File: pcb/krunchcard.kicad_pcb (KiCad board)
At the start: 2 copper layers, 86 x 54 mm, 27 parts, among them U1 NT3H2111W0FTTJ

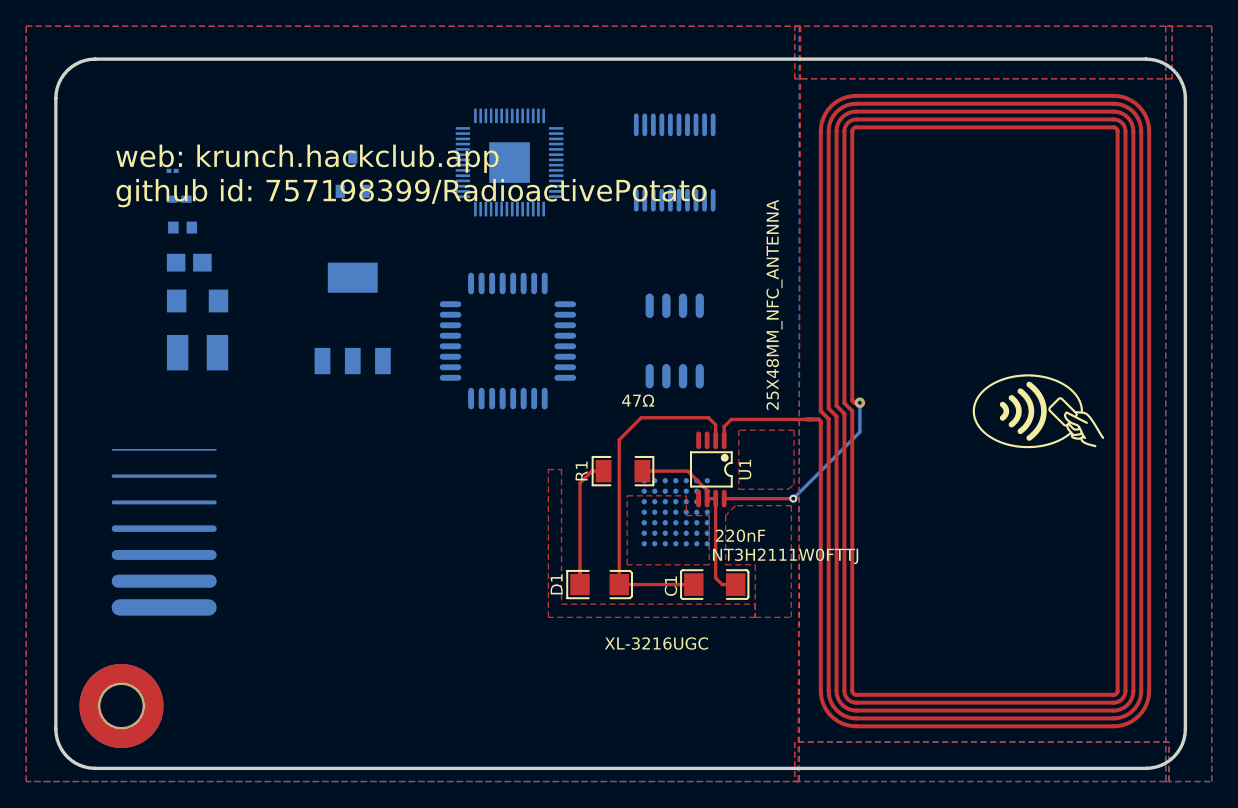
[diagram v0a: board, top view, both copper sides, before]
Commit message: updated back of pcb
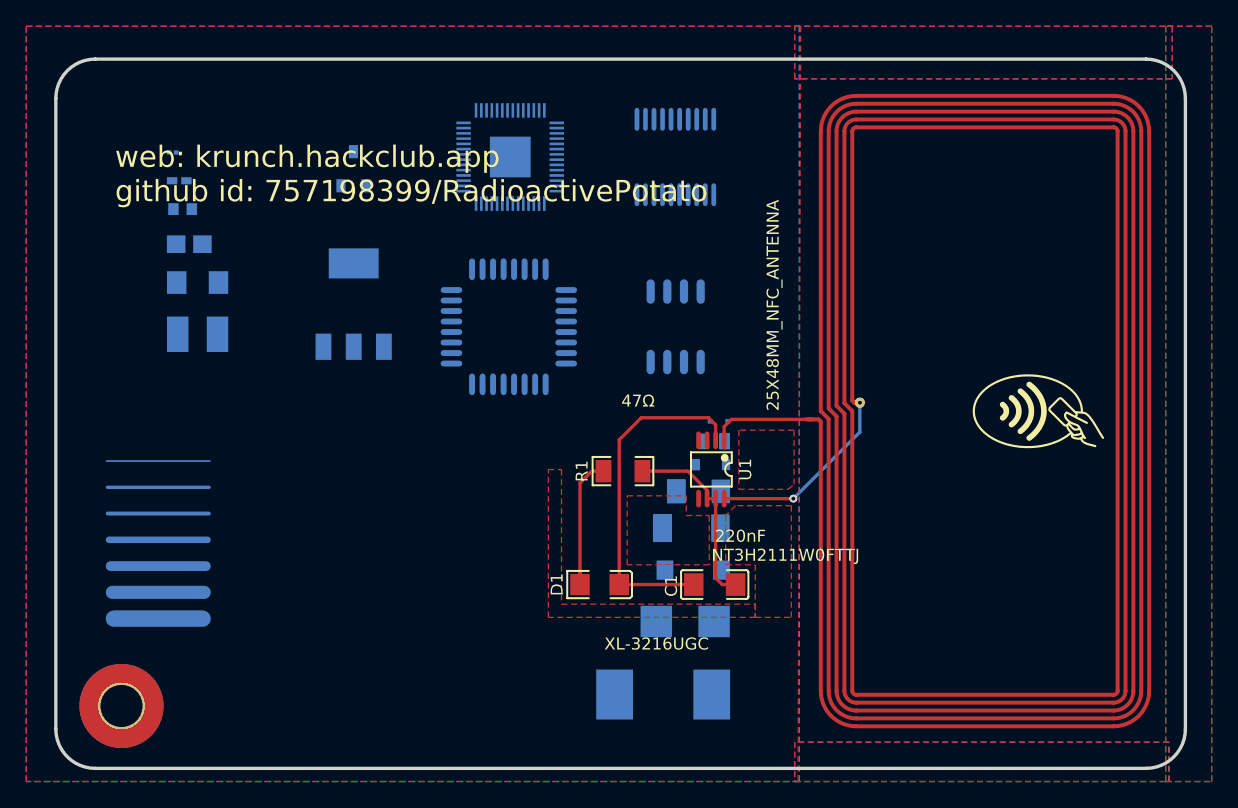
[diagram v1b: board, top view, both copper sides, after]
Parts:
- removed BGA: Analog_BGA-49_6.25x6.25mm_Layout7x7_P0.8mm, Package_BGA:Analog_BGA-49_6.25x6.25mm_Layout7x7_P0.8mm
- added ?: , , B.Cu at (158.7, 110.9)
- added ?: , , B.Cu at (156.2, 115.7)
- added ?: , , B.Cu at (160.9, 109.1)
- added ?: , , B.Cu at (157.2, 112.9)
- added E$41: , Adafruit PCB Reference Ruler:MICROMELF-R, B.Cu at (160.1, 109.1)
- added E$42: , Adafruit PCB Reference Ruler:SC79_INFINEON, B.Cu at (160.5, 107.6)
- added E$43: , Adafruit PCB Reference Ruler:SMA-DIODE, B.Cu at (158.5, 118.9)
- added E$44: , Adafruit PCB Reference Ruler:SMB-DIODE, B.Cu at (157.9, 122.8)
- added E$45: , Adafruit PCB Reference Ruler:SMC, B.Cu at (156.2, 128.4)
- added E$47: , Adafruit PCB Reference Ruler:SOD-128, B.Cu at (158.4, 115.7)
- added E$48: , Adafruit PCB Reference Ruler:SOD-323, B.Cu at (159.9, 110.9)
- added E$49: , Adafruit PCB Reference Ruler:SOD80C, B.Cu at (158.9, 112.9)
- added E$50: , Adafruit PCB Reference Ruler:NMOS-SYMB, B.Cu at (134.4, 123.6)
- added E$51: , Adafruit PCB Reference Ruler:PMOS-SYMB, B.Cu at (141.2, 123.6)
- added E$54: , Adafruit PCB Reference Ruler:NPN-SYMB, B.Cu at (134.4, 114.9)
- added E$59: , Adafruit PCB Reference Ruler:PNP-SYMB, B.Cu at (141.2, 115.0)
- moved 0402 1.40 mm to (119.4, 89.3)
- moved 1206 1.40 mm to (120.8, 97.0)
- moved 1210 1.40 mm to (120.8, 100.9)
- moved 0201 1.40 mm to (118.9, 87.1)
- moved 0603 1.40 mm to (119.7, 91.4)
- moved 0805 1.40 mm to (120.2, 94.1)
- moved QFP 1.09 mm to (144.5, 100.4)
- moved SOIC 1.09 mm to (157.2, 100.4)
- moved SOT223 1.09 mm to (132.7, 98.7)
- moved Pad_gge145080 0.96 mm to (117.8, 112.6)
- moved Pad_gge145083 0.96 mm to (117.8, 110.6)
- moved Pad_gge145086 0.96 mm to (117.8, 114.6)
- moved Pad_gge145089 0.96 mm to (117.8, 116.6)
- moved Pad_gge145092 0.96 mm to (117.8, 118.6)
- moved Pad_gge145095 0.96 mm to (117.8, 120.6)
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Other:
- board text added: "MicroMELF"
- board text added: "MiniMELF"
- board text added: "SC79"
- board text added: "SMA"
- board text added: "SMB"
- board text added: "SMC"
- board text added: "SOD128"
- board text added: "SOD323"
- board text added: "SOD80"
